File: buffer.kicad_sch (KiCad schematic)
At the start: 15 parts, among them U2 OPA377xxDBVx

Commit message: Big commit for the day
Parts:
- renumbered C4 to C?, C5 to C?, CB4 to CB?, R11 to R?, R12 to R?, R2 to R?, R3 to R?, R4 to R?, R5 to R?, R6 to R?, R7 to R?, R8 to R?, R9 to R?, R10 to R?, U2 to U?
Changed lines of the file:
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@@
   (symbol (lib_id "Device:C_Small") (at 111.76 59.69 270) (unit 1)
     (in_bom yes) (on_board yes) (dnp no)
-    (property "Reference" "C4" (at 111.76 53.8734 90)
+    (property "Reference" "C?" (at 111.76 53.8734 90)
       (effects (font (size 1.27 1.27)))
     )
@@
   (symbol (lib_id "grootvoet:OPA377xxDBVx") (at 137.16 74.93 0) (unit 1)
     (in_bom yes) (on_board yes) (dnp no)
-    (property "Reference" "U2" (at 149.86 78.74 0)
+    (property "Reference" "U?" (at 149.86 78.74 0)
       (effects (font (size 1.27 1.27)) (justify left))
     )
@@
   (symbol (lib_id "Device:R_Small") (at 118.11 59.69 90) (unit 1)
     (in_bom yes) (on_board yes) (dnp no)
-    (property "Reference" "R11" (at 116.9416 58.1914 0)
+    (property "Reference" "R?" (at 116.9416 58.1914 0)
       (effects (font (size 1.27 1.27)) (justify left))
     )
@@
   (symbol (lib_id "Device:R_Small") (at 142.24 59.69 90) (unit 1)
     (in_bom yes) (on_board yes) (dnp no)
-    (property "Reference" "R12" (at 138.43 58.42 90)
+    (property "Reference" "R?" (at 138.43 58.42 90)
       (effects (font (size 1.27 1.27)) (justify left))
     )
@@
   (symbol (lib_id "Device:C_Small") (at 142.24 49.53 270) (unit 1)
     (in_bom yes) (on_board yes) (dnp no)
-    (property "Reference" "C5" (at 146.05 50.8 90)
+    (property "Reference" "C?" (at 146.05 50.8 90)
       (effects (font (size 1.27 1.27)))
     )
@@
   (symbol (lib_id "Device:C_Small") (at 140.97 109.22 0) (unit 1)
     (in_bom yes) (on_board yes) (dnp no)
-    (property "Reference" "CB4" (at 143.3068 108.0516 0)
+    (property "Reference" "CB?" (at 143.3068 108.0516 0)
       (effects (font (size 1.27 1.27)) (justify left))
     )
@@
   (symbol (lib_id "Device:R_Small") (at 97.79 77.47 90) (unit 1)
     (in_bom yes) (on_board yes) (dnp no)
-    (property "Reference" "R2" (at 96.6216 75.9714 0)
+    (property "Reference" "R?" (at 96.6216 75.9714 0)
       (effects (font (size 1.27 1.27)) (justify left))
     )
@@
   (symbol (lib_id "Device:R_Small") (at 97.79 85.09 90) (unit 1)
     (in_bom yes) (on_board yes) (dnp no)
-    (property "Reference" "R3" (at 96.6216 83.5914 0)
+    (property "Reference" "R?" (at 96.6216 83.5914 0)
       (effects (font (size 1.27 1.27)) (justify left))
     )
@@
   (symbol (lib_id "Device:R_Small") (at 97.79 92.71 90) (unit 1)
     (in_bom yes) (on_board yes) (dnp no)
-    (property "Reference" "R4" (at 96.6216 91.2114 0)
+    (property "Reference" "R?" (at 96.6216 91.2114 0)
       (effects (font (size 1.27 1.27)) (justify left))
     )
@@
   (symbol (lib_id "Device:R_Small") (at 97.79 100.33 90) (unit 1)
     (in_bom yes) (on_board yes) (dnp no)
-    (property "Reference" "R5" (at 96.6216 98.8314 0)
+    (property "Reference" "R?" (at 96.6216 98.8314 0)
       (effects (font (size 1.27 1.27)) (justify left))
     )
@@
   (symbol (lib_id "Device:R_Small") (at 97.79 107.95 90) (unit 1)
     (in_bom yes) (on_board yes) (dnp no)
-    (property "Reference" "R6" (at 96.6216 106.4514 0)
+    (property "Reference" "R?" (at 96.6216 106.4514 0)
       (effects (font (size 1.27 1.27)) (justify left))
     )
@@
   (symbol (lib_id "Device:R_Small") (at 97.79 115.57 90) (unit 1)
     (in_bom yes) (on_board yes) (dnp no)
-    (property "Reference" "R7" (at 96.6216 114.0714 0)
+    (property "Reference" "R?" (at 96.6216 114.0714 0)
       (effects (font (size 1.27 1.27)) (justify left))
     )
@@
   (symbol (lib_id "Device:R_Small") (at 97.79 123.19 90) (unit 1)
     (in_bom yes) (on_board yes) (dnp no)
-    (property "Reference" "R8" (at 96.6216 121.6914 0)
+    (property "Reference" "R?" (at 96.6216 121.6914 0)
       (effects (font (size 1.27 1.27)) (justify left))
     )
@@
   (symbol (lib_id "Device:R_Small") (at 97.79 130.81 90) (unit 1)
     (in_bom yes) (on_board yes) (dnp no)
-    (property "Reference" "R9" (at 96.6216 129.3114 0)
+    (property "Reference" "R?" (at 96.6216 129.3114 0)
       (effects (font (size 1.27 1.27)) (justify left))
     )
@@
   (symbol (lib_id "Device:R_Small") (at 97.79 147.32 90) (unit 1)
     (in_bom yes) (on_board yes) (dnp no)
-    (property "Reference" "R10" (at 96.6216 145.8214 0)
-      (effects (font (size 1.27 1.27)) (justify left))
-    )
+    (property "Reference" "R?" (at 96.6216 145.8214 0)
+      (effects (font (size 1.27 1.27)) (justify left))
+    )

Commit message: (bc) large commit with spice experiments
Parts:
- removed R? (x7): 2k2, Resistor_SMD:R_0603_1608Metric_Pad0.98x0.95mm_HandSolder, symbol Device:R_Small
- added R63, R64, R65, R66, R67, R68, R69: 200, Resistor_SMD:R_0603_1608Metric_Pad0.98x0.95mm_HandSolder, symbol Device:R_Small
- R62: renamed from R?; value 2k2 -> 200; MPN ERJ-3EKF2201V -> (none)
- R70: renamed from R?; value PH -> 2.2k
- gave numbers to parts that had none: 6
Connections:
- net IN1: now also R63.1
- net IN2: now also R64.1
- net IN3: now also R65.1
- net IN4: now also R66.1
- net IN5: now also R67.1
- net IN6: now also R68.1
- net IN7: now also R69.1
- net at R62.2, R70.2, U8.3 (+): now also R63.2, R64.2, R65.2, R66.2, R67.2, R68.2, R69.2
- net GND renamed 0

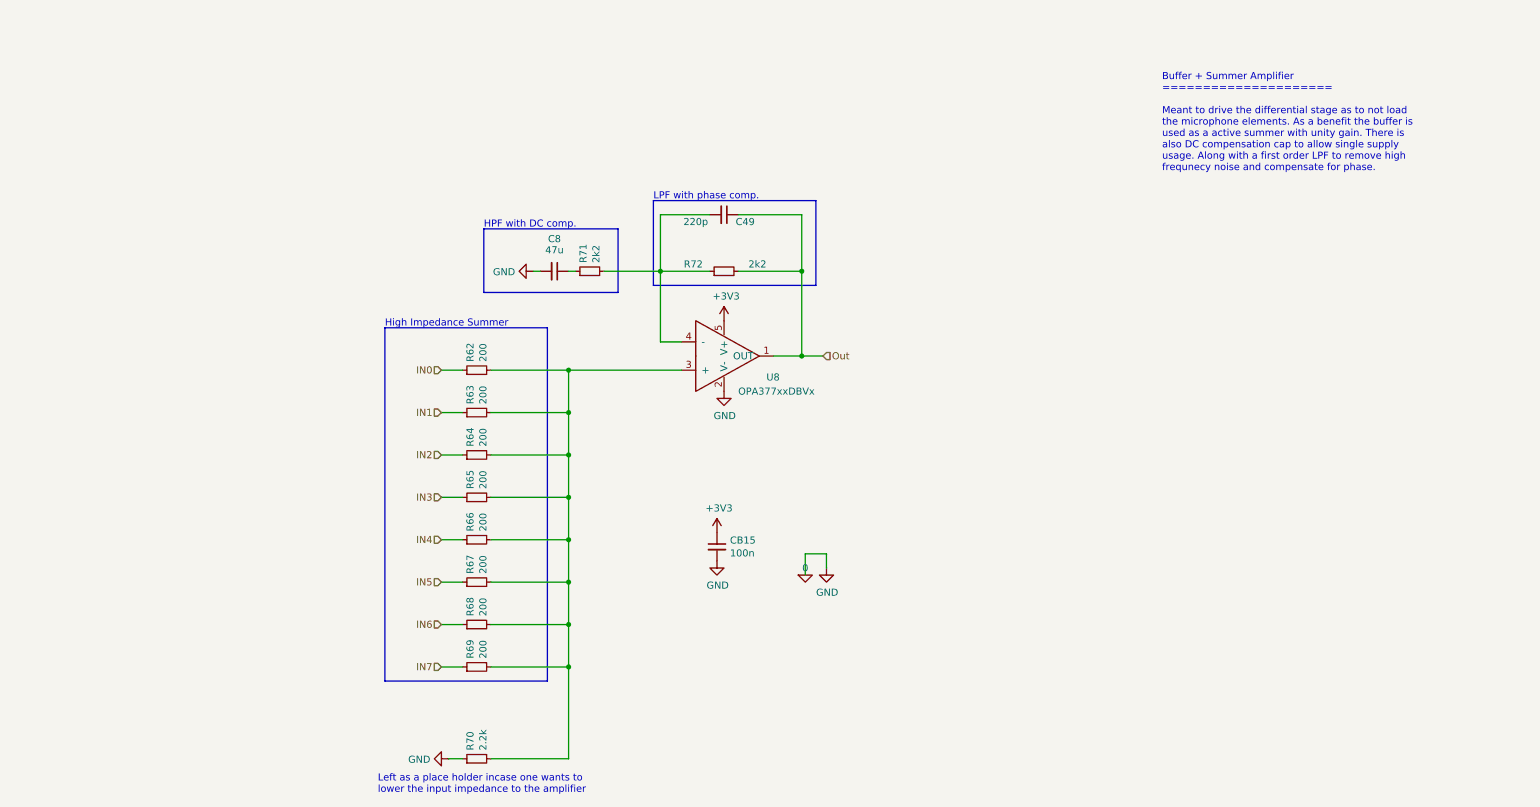
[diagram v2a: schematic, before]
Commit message: (bc) new summation preamp & seperate power net
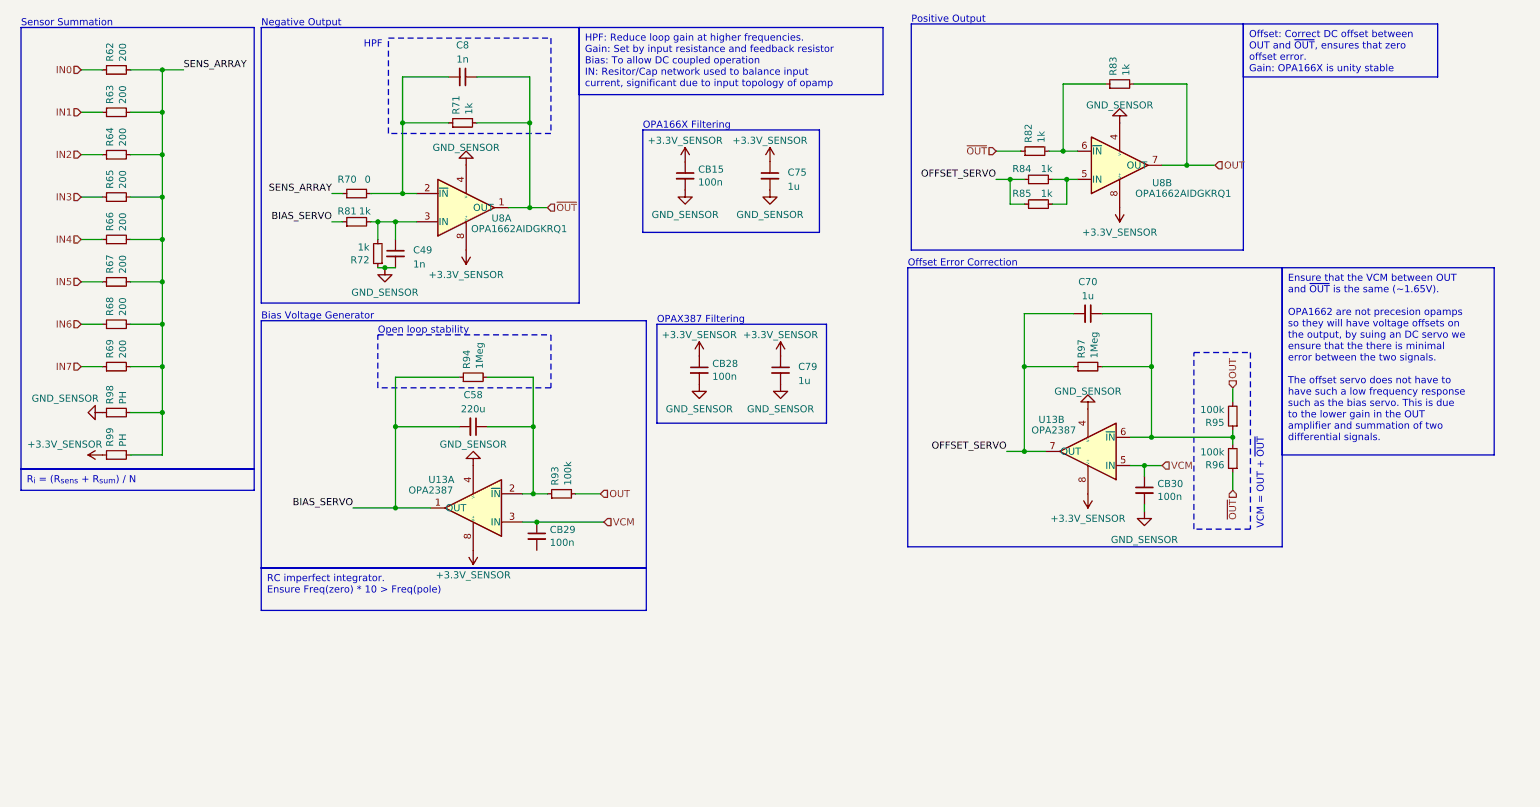
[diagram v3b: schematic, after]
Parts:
- removed U8: OPA377xxDBVx, Package_TO_SOT_SMD:SOT-23-5, symbol grootvoet:OPA377xxDBVx
- added C58: 220u, symbol Device:C_Small
- added C70, C75, C79: 1u, symbol Device:C_Small
- added CB28, CB29, CB30: 100n, Capacitor_SMD:C_0603_1608Metric_Pad1.08x0.95mm_HandSolder, symbol Device:C_Small
- added R81, R82, R83, R84, R85: 1k, Resistor_SMD:R_0603_1608Metric_Pad0.98x0.95mm_HandSolder, symbol Device:R_Small
- added R93, R95, R96: 100k, Resistor_SMD:R_0603_1608Metric_Pad0.98x0.95mm_HandSolder, symbol Device:R_Small
- added R94, R97: 1Meg, Resistor_SMD:R_0603_1608Metric_Pad0.98x0.95mm_HandSolder, symbol Device:R_Small
- added R98, R99: PH, Resistor_SMD:R_0603_1608Metric_Pad0.98x0.95mm_HandSolder, symbol Device:R_Small
- added U13: OPA2387, grootvoet:OPA1662AIDGK, symbol grootvoet:OPA2387
- added U8: OPA1662AIDGKRQ1, grootvoet:OPA1662AIDGK, symbol grootvoet:OPA1662
- C49: value 220p -> 1n; footprint Capacitor_SMD:C_0603_1608Metric_Pad1.08x0.95mm_HandSolder -> (none); MPN C0603C221J5GACTU -> (none); Mfr. KEMET -> (none)
- C8: value 47u -> 1n; footprint Capacitor_SMD:C_1206_3216Metric_Pad1.33x1.80mm_HandSolder -> (none); MPN GRM31CR60J107KE39K -> (none); Mfr. Murata Electronics -> (none); Notes Specified 47u but that is min. (>47u is better) -> (none)
- R70: value 2.2k -> 0; Mfr. (none) -> Panasonic
- R71, R72: value 2k2 -> 1k; MPN ERJ-3EKF2201V -> (none)
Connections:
- net at R71.1: now also C8.2, R70.2, U8.2 (~{IN}); no longer C8.1
- net SENS_ARRAY: now reaches R62.2, R63.2, R64.2, R65.2, R66.2, R67.2, R68.2, R69.2
- net SENS_ARRAY: now also R70.1, R98.2, R99.2; no longer R70.2
- net GND: now reaches C49.2, R72.1
- net GND: now also CB15.2, C75.2, C79.2, CB28.2, CB30.2, R98.1, U13.4 (V-), U13.4 (V-), U8.4 (V-), U8.4 (V-); no longer R71.2
- net +3V3 renamed +3.3V
- net +3.3V: now also C75.1, C79.1, CB28.1, R99.1, U13.8 (V+), U13.8 (V+), U8.8 (V+), U8.8 (V+)
- removed net 0: C8.2, CB15.2, R70.1
- net Out: no longer names the net of C49.1, R72.2
- net Out: now also R81.2, U8.3 (IN)
- new net: C70.1, R95.1, R96.2, R97.2, U13.6 (~{IN})
- new net: R84.2, R85.2, U8.5 (IN)
- new net: R82.2, R83.1, U8.6 (~{IN})
- new net: C58.1, R93.1, R94.2, U13.2 (~{IN})
- new net BIAS_SERVO: C58.2, R81.1, R94.1, U13.1 (OUT)
- new net OFFSET_SERVO: C70.2, R84.1, R85.1, R97.1, U13.7 (OUT)
- new net OUT: R83.2, R93.2, R95.2, U8.7 (OUT)
- new net VCM: CB29.1, CB30.1, U13.3 (IN), U13.5 (IN)
- new net ~{OUT}: C8.1, R71.2, R82.1, R96.1, U8.1 (OUT)
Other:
- note added: "Bias Voltage Generator"
- note added: "HPF"
- note added: "Negative Output"
- note added: "OPA166X Filtering"
- note added: "OPAX387 Filtering"
- note added: "Offset Error Correction"
- note added: "Open loop stability"
- note added: "Positive Output"
- note added: "Sensor Summation"
- note added: "VCM = OUT + ~{OUT}"
- note removed: "Buffer + Summer Amplifier ===================== Meant to drive the differential stage as to not load the microphone elements. As a benefit the buffer is used as a active summer with unity gain. There is also DC compensation cap to allow single supply usage. Along with a first order LPF to remove high frequnecy noise and compensate for phase."
- note removed: "HPF with DC comp."
- note removed: "High Impedance Summer"
- note removed: "LPF with phase comp."
- note removed: "Left as a place holder incase one wants to lower the input impedance to the amplifier"
- moved on the sheet: CB15, R62, R63, R64, R65, R66, R67, R68, R69

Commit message: (bc) changes for the day
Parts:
- R98, R99: now not fitted; now left out of the parts list
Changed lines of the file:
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@@
   )
   (symbol (lib_id "Device:R_Small") (at 33.02 92.71 90) (unit 1)
-    (in_bom yes) (on_board yes) (dnp no)
+    (in_bom no) (on_board yes) (dnp yes)
     (property "Reference" "R99" (at 31.8516 91.2114 0)
       (effects (font (size 1.27 1.27)) (justify left))
@@
   )
   (symbol (lib_id "Device:R_Small") (at 33.02 85.09 90) (unit 1)
-    (in_bom yes) (on_board yes) (dnp no)
+    (in_bom no) (on_board yes) (dnp yes)
     (property "Reference" "R98" (at 31.8516 83.5914 0)
       (effects (font (size 1.27 1.27)) (justify left))

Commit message: (sch) relabel
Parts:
- renumbered C49 to C1401, C8 to C1402, C58 to C1403, C75 to C1404, C79 to C1405, C70 to C1406, CB29 to CB1401, CB15 to CB1402, CB28 to CB1403, CB30 to CB1404, R62 to R1401, R63 to R1402, R64 to R1403, R65 to R1404, R66 to R1405, R67 to R1406, R68 to R1407, R69 to R1408, R98 to R1409, R99 to R1410, R70 to R1411, R81 to R1412, R72 to R1413, R71 to R1414, R94 to R1415, R93 to R1416, R82 to R1417, R84 to R1418, R85 to R1419, R97 to R1420, R83 to R1421, R95 to R1422, R96 to R1423, U8 to U1401, U13 to U1402

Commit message: (bc) finish up ERC
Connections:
- net GND: now also CB1401.2
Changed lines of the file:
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@@
     (fill (type none))
   )
-  (rectangle (start 59.055 68.58) (end 128.27 113.03)
+  (rectangle (start 59.69 68.58) (end 128.27 116.205)
     (stroke (width 0) (type default))
     (fill (type none))
@@
   )
   (text_box "RC imperfect integrator. \nEnsure Freq(zero) * 10 > Freq(pole)"
-    (at 59.055 113.03 0) (size 69.215 7.62)
+    (at 59.055 116.205 0) (size 69.215 7.62)
     (stroke (width 0) (type default))
     (fill (type none))
@@
         )
       )
+    )
+  )
+  (symbol (lib_id "grootvoet:GND_SENSOR") (at 108.585 109.855 0) (unit 1)
+    (in_bom yes) (on_board yes) (dnp no)
+    (property "Reference" "#PWR0215" (at 108.585 116.205 0)
+      (effects (font (size 1.27 1.27)) hide)
+    )
+    (property "Value" "GND_SENSOR" (at 113.03 114.3 0)
+      (effects (font (size 1.27 1.27)))
+    )
+    (property "Footprint" "" (at 108.585 109.855 0)
+      (effects (font (size 1.27 1.27)) hide)
+    )
+    (property "Datasheet" "" (at 108.585 109.855 0)
+      (effects (font (size 1.27 1.27)) hide)
+    )
+    (pin "1")
+    (instances
+      (project "kleinvoet"
+        (path "/4185c36c-c66e-4dbd-be5d-841e551f4885/b53619ea-788f-4bc9-9946-594014d7d22c"
+          (reference "#PWR0215") (unit 1)
+        )
+        (path "/4185c36c-c66e-4dbd-be5d-841e551f4885/b53619ea-788f-4bc9-9946-594014d7d22c/00000000-0000-0000-0000-00005f9c4001"
+          (reference "#PWR01510") (unit 1)
+        )
+      )

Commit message: (hk) asign footprints
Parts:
- C1501: renamed from C1401; footprint (none) -> Capacitor_SMD:C_0603_1608Metric_Pad1.08x0.95mm_HandSolder
- C1502: renamed from C1402; footprint (none) -> Capacitor_SMD:C_0603_1608Metric_Pad1.08x0.95mm_HandSolder
- C1503: renamed from C1403; footprint (none) -> Capacitor_SMD:C_1206_3216Metric; MPN (none) -> GRM31CC80E227ME11L; Mfr. (none) -> Murata
- C1504: renamed from C1404; footprint (none) -> Capacitor_SMD:C_0603_1608Metric_Pad1.08x0.95mm_HandSolder
- C1505: renamed from C1405; footprint (none) -> Capacitor_SMD:C_0603_1608Metric_Pad1.08x0.95mm_HandSolder
- C1506: renamed from C1406; footprint (none) -> Capacitor_SMD:C_0603_1608Metric_Pad1.08x0.95mm_HandSolder
- R1511: renamed from R1411; now not fitted; now left out of the parts list
- renumbered CB1401 to CB1501, CB1402 to CB1502, CB1403 to CB1503, CB1404 to CB1504, R1401 to R1501, R1402 to R1502, R1403 to R1503, R1404 to R1504, R1405 to R1505, R1406 to R1506, R1407 to R1507, R1408 to R1508, R1409 to R1509, R1410 to R1510, R1412 to R1512, R1413 to R1513, R1414 to R1514, R1415 to R1515, R1416 to R1516, R1417 to R1517, R1418 to R1518, R1419 to R1519, R1420 to R1520, R1421 to R1521, R1422 to R1522, R1423 to R1523, U1401 to U1501, U1402 to U1502
